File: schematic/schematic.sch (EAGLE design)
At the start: 8 parts, among them IC1 4021N, IC2 4021N

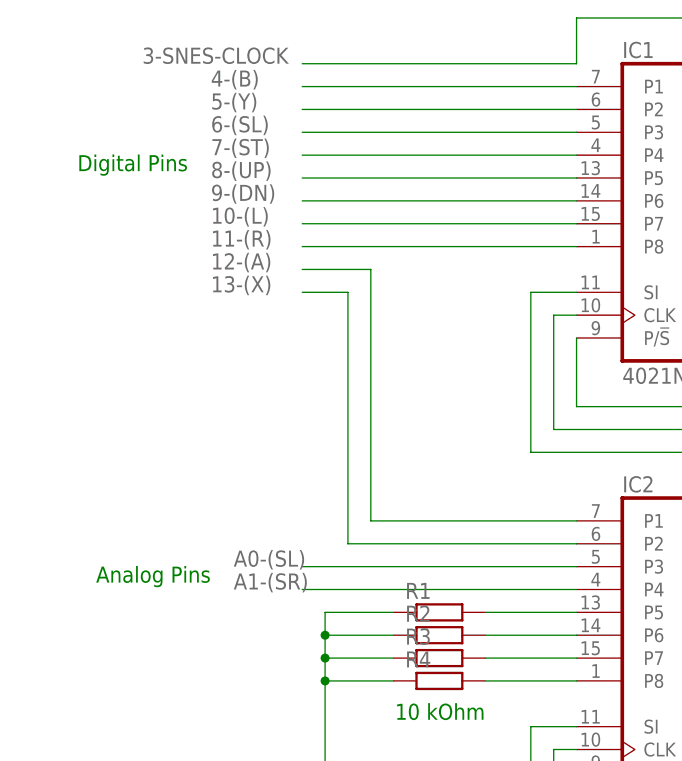
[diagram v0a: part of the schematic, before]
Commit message: Do not use pin 13 - reserved for LED
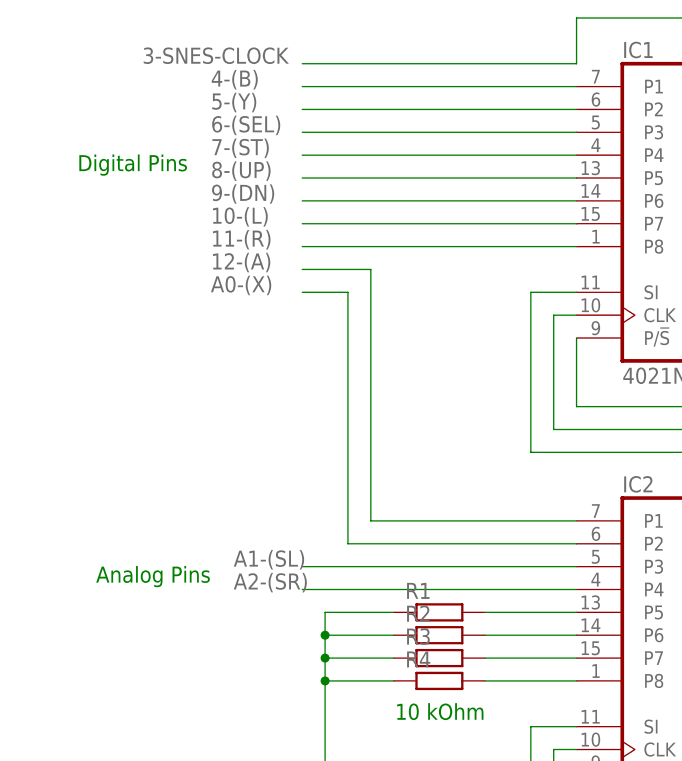
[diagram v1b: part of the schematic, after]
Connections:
- net A0-(SL) renamed A1-(SL)
- net A1-(SR) renamed A2-(SR)
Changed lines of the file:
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@@
 </segment>
 </net>
-<net name="6-(SL)" class="0">
+<net name="6-(SEL)" class="0">
 <segment>
 <wire x1="48.26" y1="76.2" x2="17.78" y2="76.2" width="0.1524" layer="91"/>
@@
 </segment>
 </net>
-<net name="13-(X)" class="0">
+<net name="A0-(X)" class="0">
 <segment>
 <wire x1="48.26" y1="30.48" x2="22.86" y2="30.48" width="0.1524" layer="91"/>
@@
 </segment>
 </net>
-<net name="A0-(SL)" class="0">
+<net name="A1-(SL)" class="0">
 <segment>
 <pinref part="IC2" gate="A" pin="P3"/>
@@
 </segment>
 </net>
-<net name="A1-(SR)" class="0">
+<net name="A2-(SR)" class="0">
 <segment>
 <pinref part="IC2" gate="A" pin="P4"/>
